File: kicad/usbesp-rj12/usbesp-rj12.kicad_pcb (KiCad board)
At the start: 2 copper layers, 15.2 x 28.6 mm, 10 parts, among them J1 USB_B_Micro, J2 RJ12, Q1 S9013, Q2 S9013, U1 FT232RL

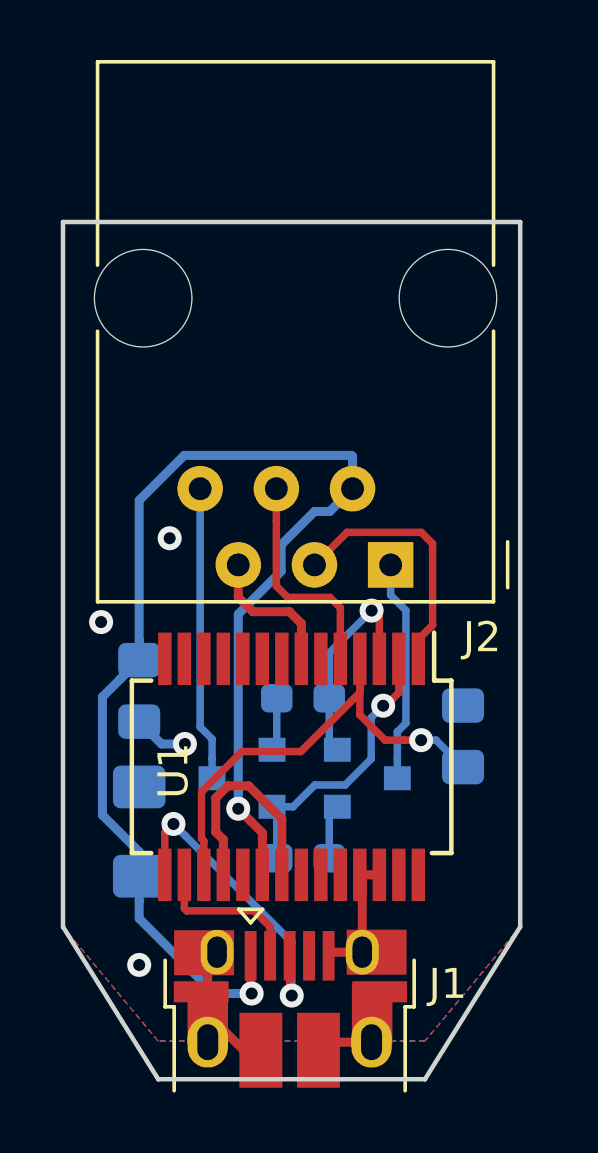
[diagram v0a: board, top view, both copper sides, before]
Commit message: USB MicroB update
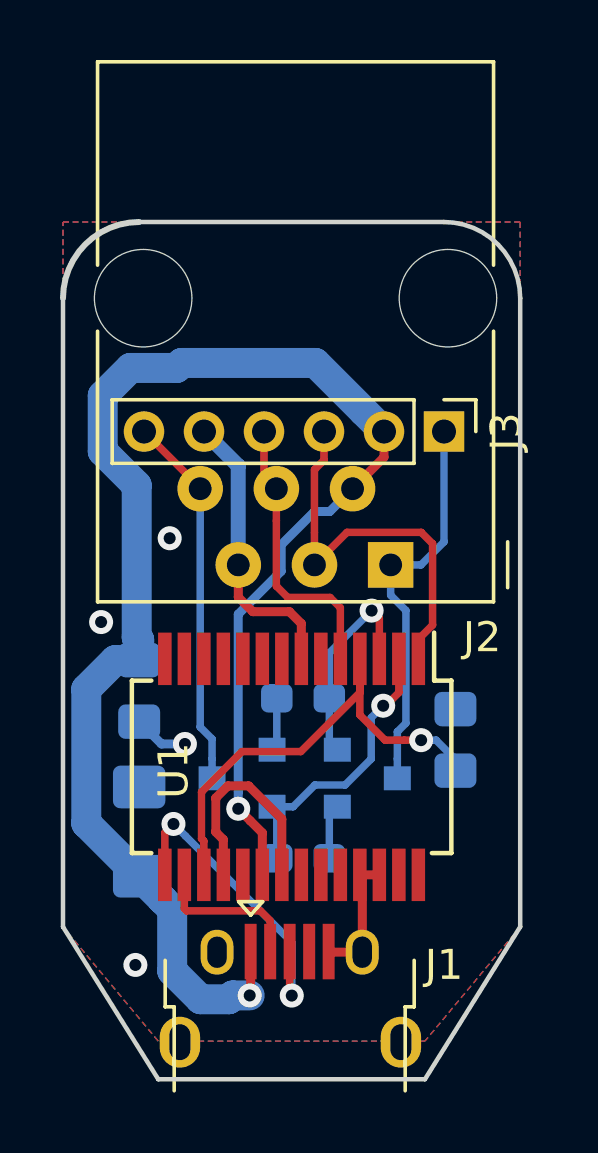
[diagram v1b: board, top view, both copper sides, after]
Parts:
- added J3: Conn_01x06, Connector_PinHeader_2.00mm:PinHeader_1x06_P2.00mm_Vertical, F.Cu at (155.6, 88.9)
- J1: footprint Connector_USB:USB_Micro-B_Amphenol_10103594-0001LF_Horizontal -> lib:USB_Micro-B_Horizontal
- moved C3 0.28 mm to (156.0, 99.2)
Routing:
- net /VBUS: track 44.9 -> 54.8 mm
- net /RESET: track 7.44 -> 13.2 mm
- net /TXD: track 8.58 -> 13.2 mm
- net /IO0: track 9.82 -> 12.5 mm
- net /RXD: track 7.38 -> 9.46 mm
- net GND: track 24.5 -> 23.1 mm
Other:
- outline, holes or cut-outs redrawn
- net class VBUS added: clearance 0.2, trace_width 1, via_dia 0.8, via_drill 0.4

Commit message: PCB improved
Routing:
- net GND: track 23.1 -> 35.2 mm, vias 4 -> 1
- net /IO0: track 12.5 -> 16.1 mm
- net /RESET: track 13.2 -> 12.6 mm
